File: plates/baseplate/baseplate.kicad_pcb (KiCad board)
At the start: 2 copper layers, 107.2 x 83.3 mm, 5 parts

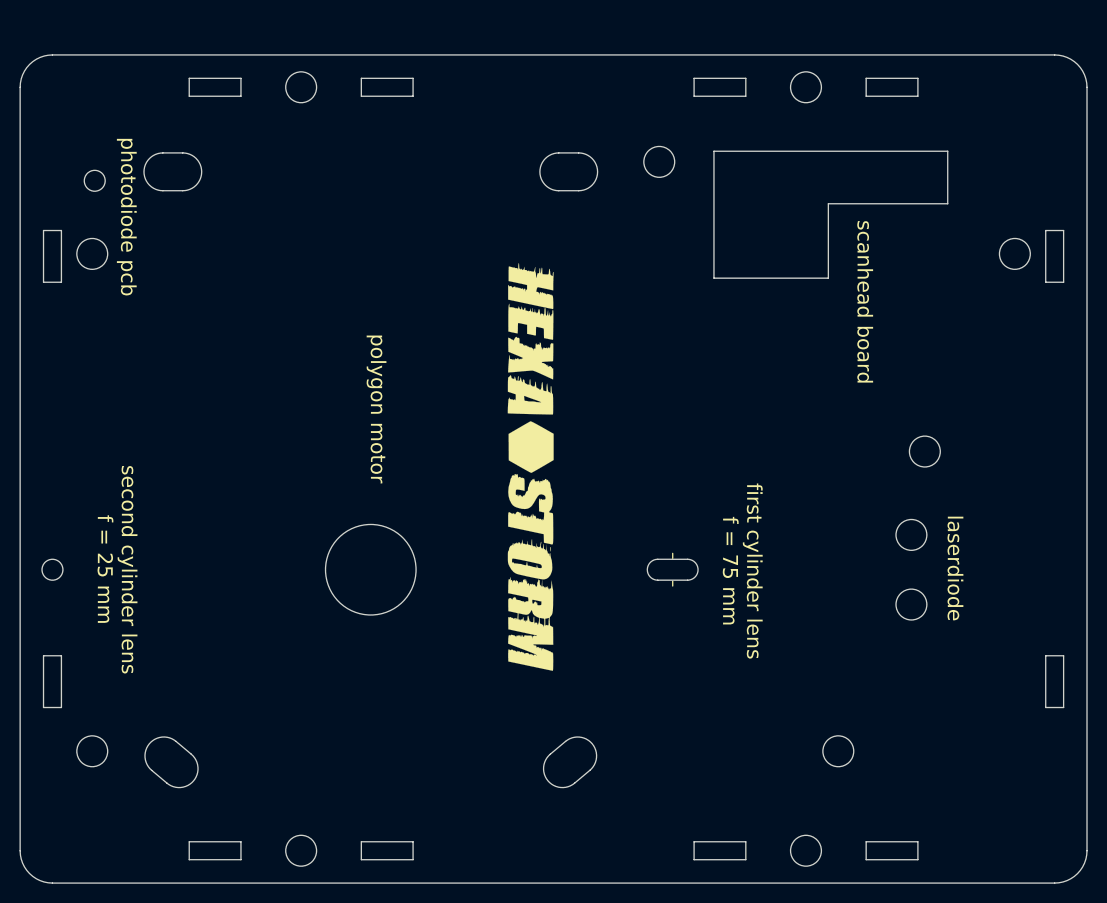
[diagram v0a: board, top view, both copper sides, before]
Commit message: improved bom changed export settings
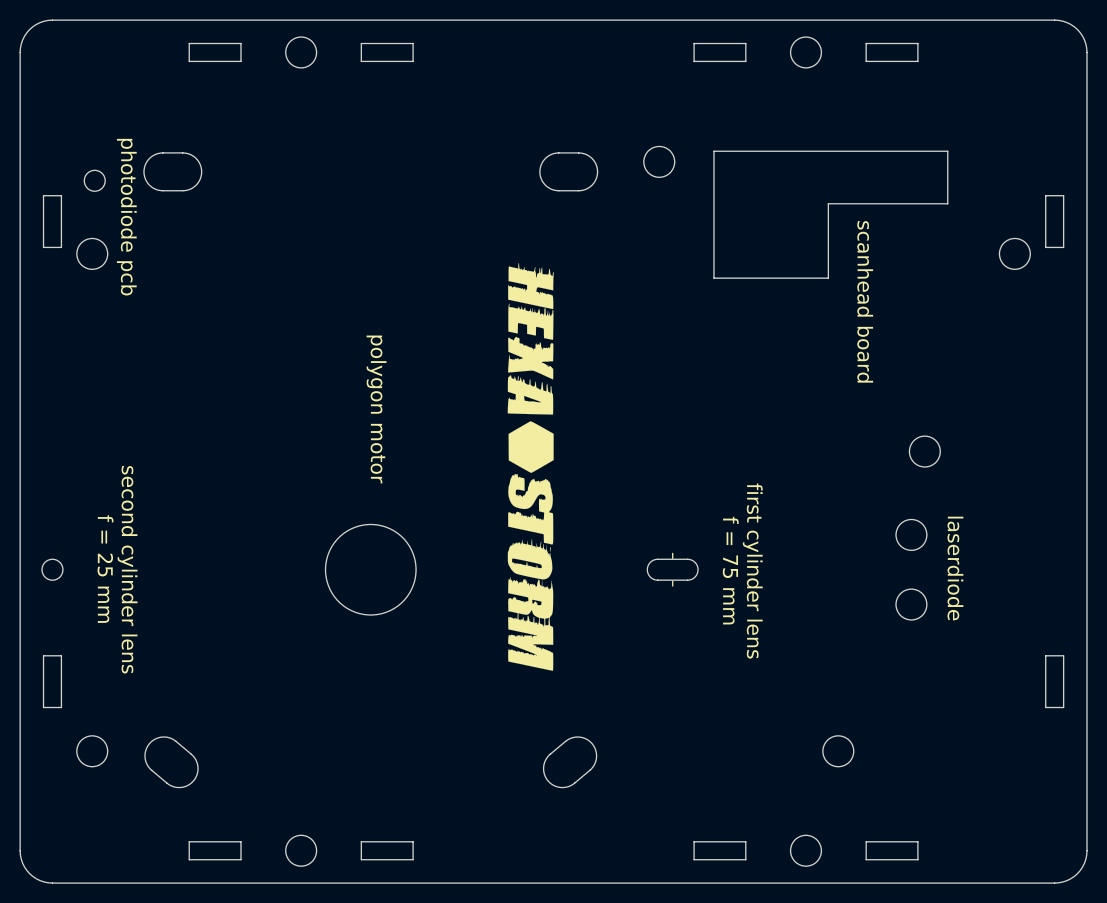
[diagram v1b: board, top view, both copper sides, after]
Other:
- board size 107.2 x 83.3 mm -> 107.2 x 86.7 mm
